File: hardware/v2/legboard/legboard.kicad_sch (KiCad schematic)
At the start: 12 parts, among them J1 UPLINK_RJ11, J2 COXA, J3 FEMUR, J4 TIBIA, J5 SERVO_PWR_IN, J6 SENSE, U1 XIAO-RP2040, U2 SP3485CN

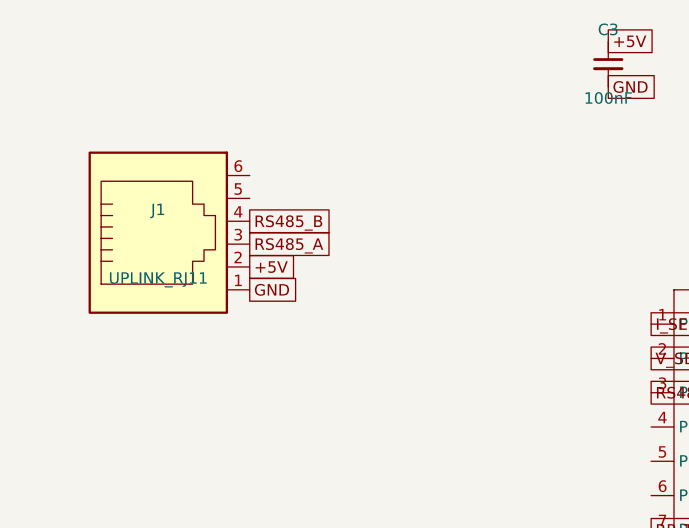
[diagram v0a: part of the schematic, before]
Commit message: move pin connection in rj11
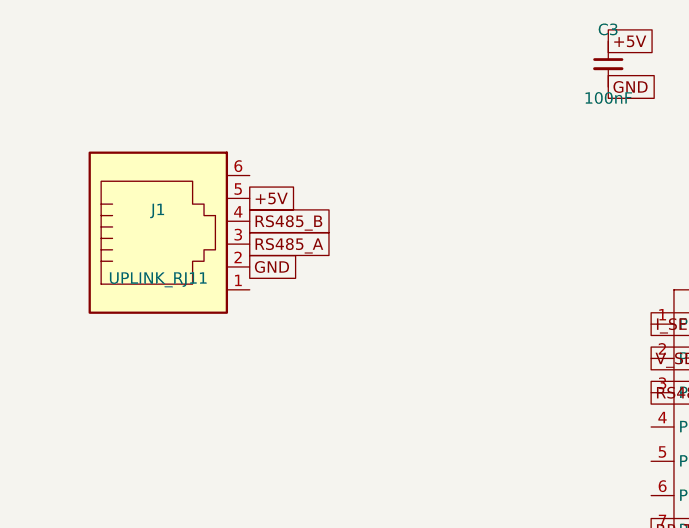
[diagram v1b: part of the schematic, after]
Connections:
- net +5V: now also J1.5; no longer J1.2
- net GND: now also J1.2; no longer J1.1
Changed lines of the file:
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@@
 	(global_label "GND"
-		(shape passive)
-		(at 60.16 95.08 0)
-		(fields_autoplaced yes)
-		(effects
-			(font
-				(size 1.27 1.27)
-			)
-			(justify left)
-		)
-	)
-	(global_label "+5V"
 		(shape passive)
 		(at 60.16 92.54 0)
@@
 		(fields_autoplaced yes)
 		(effects
+			(font
+				(size 1.27 1.27)
+			)
+			(justify left)
+		)
+	)
+	(global_label "+5V"
+		(shape passive)
+		(at 60.16 84.92 0)
+		(fields_autoplaced yes)
+		(effects

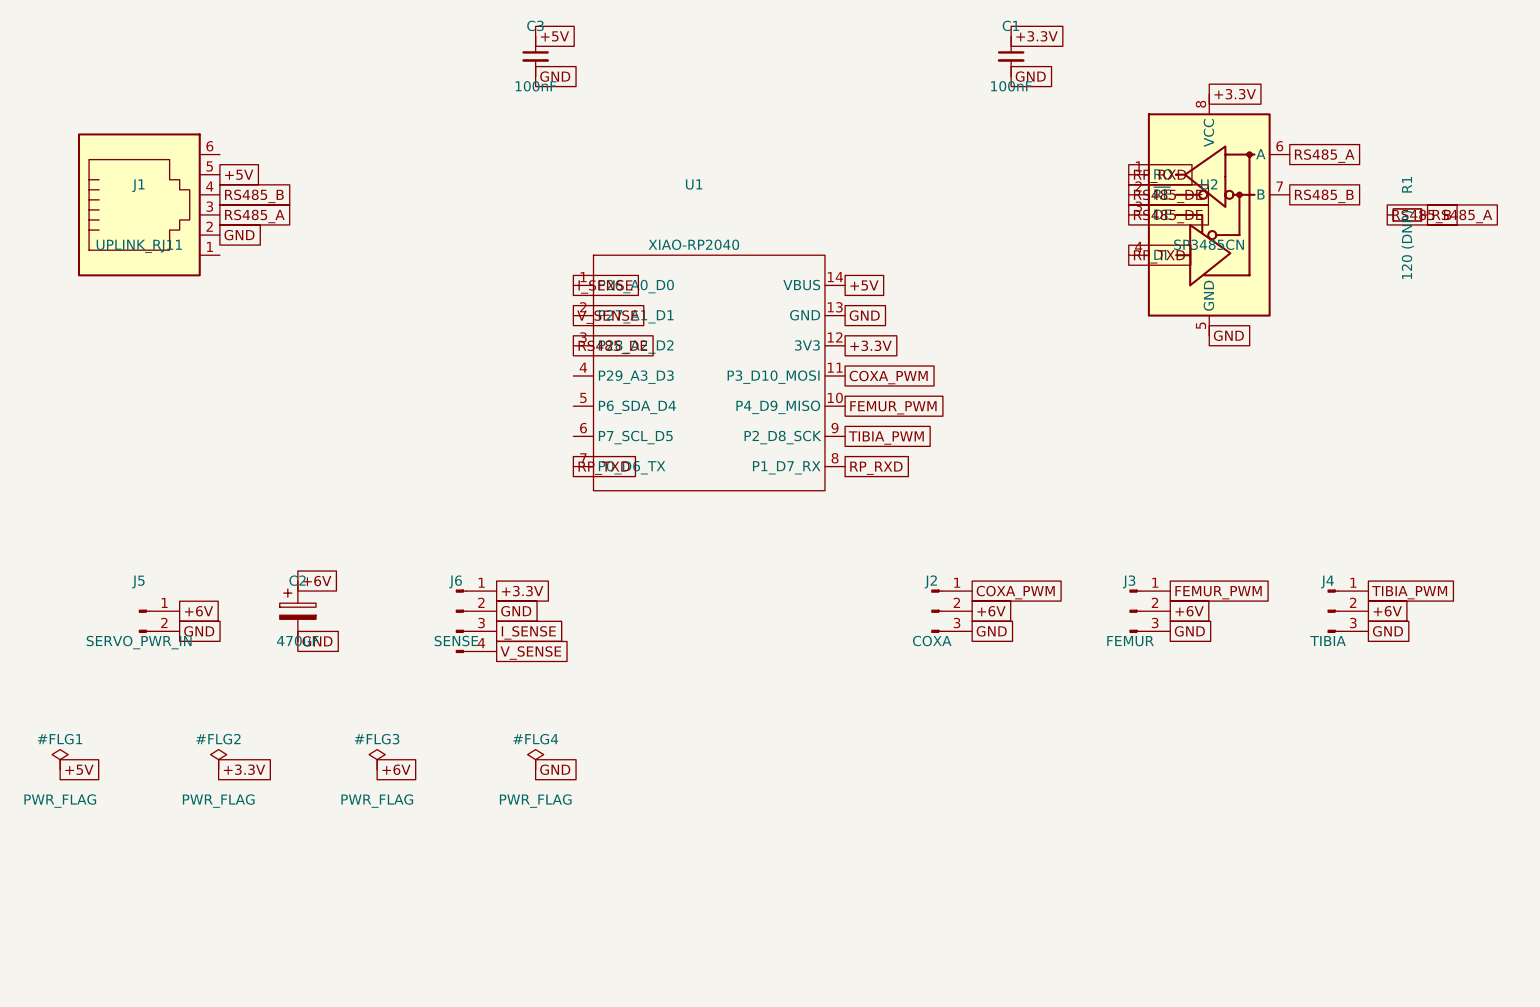
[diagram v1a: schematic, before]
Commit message: Update V2 board schematics and footprints
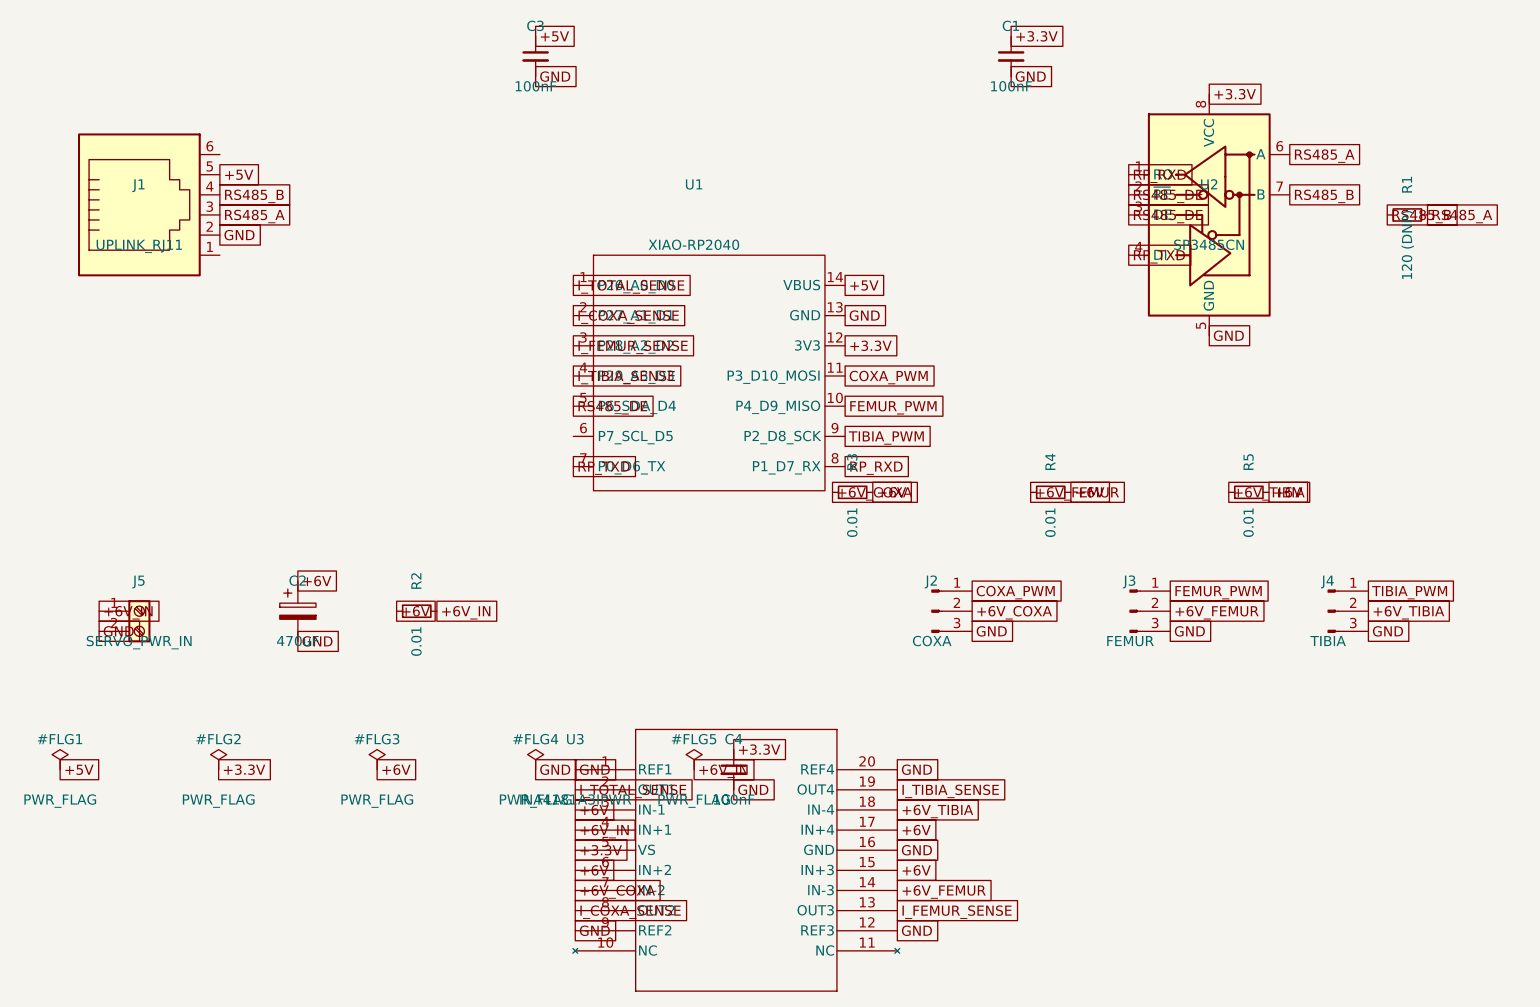
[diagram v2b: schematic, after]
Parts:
- removed J6: SENSE, symbol Connector:Conn_01x04_Pin
- added C4: 100nF, Capacitor_SMD:C_0805_2012Metric, symbol Device:C_Small
- added R2, R3, R4, R5: 0.01, Resistor_SMD:R_Shunt_Ohmite_LVK12, symbol Device:R_Small
- added U3: INA4181A3IPWR, Custom:PW20_TEX, symbol INA4181A3IPWR:INA4181A3IPWR
- C1, C3: footprint (none) -> Capacitor_SMD:C_0805_2012Metric
- C2: footprint (none) -> Capacitor_THT:CP_Radial_D8.0mm_P3.50mm
- J1: footprint (none) -> Connector_RJ:RJ25_Wayconn_MJEA-660X1_Horizontal
- J2, J3, J4: footprint (none) -> Connector_PinHeader_2.54mm:PinHeader_1x03_P2.54mm_Vertical
- J5: footprint (none) -> TerminalBlock:TerminalBlock_MaiXu_MX126-5.0-02P_1x02_P5.00mm; symbol Connector:Conn_01x02_Pin -> Connector:Screw_Terminal_01x02
- R1: footprint (none) -> Resistor_SMD:R_0805_2012Metric
- U1: footprint (none) -> Seeed_Studio_XIAO_Series:XIAO-RP2040-DIP
- U2: footprint (none) -> Package_SO:SOIC-8_3.9x4.9mm_P1.27mm
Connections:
- net +3.3V: now also C4.1, U3.5 (VS)
- net +6V: now also R2.1, R3.2, R4.2, R5.2, U3.15 (IN+3), U3.17 (IN+4), U3.3 (IN-1), U3.6 (IN+2); no longer J2.2 (Pin_2), J3.2 (Pin_2), J4.2 (Pin_2), J5.1 (Pin_1)
- net GND: now also C4.2, U3.1 (REF1), U3.12 (REF3), U3.16 (GND), U3.20 (REF4), U3.9 (REF2)
- net RS485_DE: now also U1.5 (P6_SDA_D4); no longer U1.3 (P28_A2_D2)
- net I_TIBIA_SENSE: now reaches U1.4 (P29_A3_D3)
- net I_TIBIA_SENSE: now also U3.19 (OUT4)
- net I_SENSE renamed I_TOTAL_SENSE
- net I_TOTAL_SENSE: now also U3.2 (OUT1)
- net V_SENSE renamed I_COXA_SENSE
- net I_COXA_SENSE: now also U3.8 (OUT2)
- new net +6V_COXA: J2.2 (Pin_2), R3.1, U3.7 (IN-2)
- new net +6V_FEMUR: J3.2 (Pin_2), R4.1, U3.14 (IN-3)
- new net +6V_IN: J5.1 (Pin_1), R2.2, U3.4 (IN+1)
- new net +6V_TIBIA: J4.2 (Pin_2), R5.1, U3.18 (IN-4)
- new net I_FEMUR_SENSE: U1.3 (P28_A2_D2), U3.13 (OUT3)

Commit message: Use 1210 footprint for legboard shunts
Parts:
- R2, R3, R4, R5: footprint Resistor_SMD:R_Shunt_Ohmite_LVK12 -> Resistor_SMD:R_1210_3225Metric_Pad1.30x2.65mm_HandSolder
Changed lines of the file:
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@@
 			)
 		)
-		(property "Footprint" "Resistor_SMD:R_Shunt_Ohmite_LVK12"
+		(property "Footprint" "Resistor_SMD:R_1210_3225Metric_Pad1.30x2.65mm_HandSolder"
 			(at 85 140 0)
 			(effects
@@
 			)
 		)
-		(property "Footprint" "Resistor_SMD:R_Shunt_Ohmite_LVK12"
+		(property "Footprint" "Resistor_SMD:R_1210_3225Metric_Pad1.30x2.65mm_HandSolder"
 			(at 140 125 0)
 			(effects
@@
 			)
 		)
-		(property "Footprint" "Resistor_SMD:R_Shunt_Ohmite_LVK12"
+		(property "Footprint" "Resistor_SMD:R_1210_3225Metric_Pad1.30x2.65mm_HandSolder"
 			(at 165 125 0)
 			(effects
@@
 			)
 		)
-		(property "Footprint" "Resistor_SMD:R_Shunt_Ohmite_LVK12"
+		(property "Footprint" "Resistor_SMD:R_1210_3225Metric_Pad1.30x2.65mm_HandSolder"
 			(at 190 125 0)
 			(effects
